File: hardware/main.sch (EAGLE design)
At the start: 37 parts, among them U1 TMS320F28069_PN_80, U10 TXB0101_DBV_6, U2 TXB0101_DBV_6, U3 TS3A5018_PW_16, U4 TS3A5018_PW_16, U5 SN74LVC4245A_DW_24, U7 Value, U8 Value, U9 SN74LVC4245A_DW_24

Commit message: Finished schematic, laid out board
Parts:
- removed EXTCON2: M10SILK_FEMALE_PTH, SparkFun-Connectors:M10SILK_FEMALE_PTH
- added JP3: M10SILK_FEMALE_PTH, SparkFun-Connectors:M10SILK_FEMALE_PTH
- added U$4, U$8: 8PIN_SOCKET, ControllerCard:8PIN_SOCKET
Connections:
- removed net IBUFIN1: U7.1A1
- removed net IBUFIN2: U7.1A2
- removed net IBUFIN3: U7.1A3
- removed net IBUFIN4: U7.1A4
- removed net IBUFIN5: U7.2A1
- removed net IBUFIN6: U7.2A2
- removed net IBUFIN7: U7.2A3
- removed net IBUFIN8: U7.2A4
- removed net OBUFIN1: U8.1Y1
- removed net OBUFIN2: U8.1Y2
- removed net OBUFIN3: U8.1Y3
- removed net OBUFIN4: U8.1Y4
- removed net OBUFIN5: U8.2Y1
- removed net OBUFIN6: U8.2Y2
- removed net OBUFIN7: U8.2Y3
- removed net OBUFIN8: U8.2Y4
- new net N$13: U$4.1, U8.1Y1
- new net N$14: U$4.2, U8.1Y2
- new net N$15: U$4.3, U8.1Y3
- new net N$16: U$4.4, U8.1Y4
- new net N$17: U$4.8, U8.2Y4
- new net N$18: U$4.7, U8.2Y3
- new net N$19: U$4.6, U8.2Y2
- new net N$20: U$4.5, U8.2Y1
- new net N$21: U$8.1, U7.1A1
- new net N$22: U$8.2, U7.1A2
- new net N$23: U$8.3, U7.1A3
- new net N$24: U$8.4, U7.1A4
- new net N$25: U$8.8, U7.2A4
- new net N$26: U$8.7, U7.2A3
- new net N$27: U$8.6, U7.2A2
- new net N$28: U$8.5, U7.2A1
- net !FLASHEN!: now also U1.GPIO22/EQEP1S/MCLKXA/SCITXDB; no longer U1.GPIO7/EPWM4B/SCIRXDA/ECAP2
- net !FLASHHOLD!: now also U1.GPIO33/SCLA/EPWMSYNCO/*ADCSOCBO; no longer U1.GPIO6/EPWM4A/EPWMSYNCI/EPWMSYNCO
- net !FLASHWP!: now also U1.GPIO32/SDAA/EPWMSYNCI/*ADCSOCAO; no longer U1.GPIO8/EPWM5A/*ADCSOCAO
- net 3.3V: no longer EXTCON2.1
- net 5V: now also JP3.10
- net BIN1: no longer EXTCON1.4
- net BIN2: no longer EXTCON1.6
- net BIN3: no longer EXTCON1.8
- net BIN4: no longer EXTCON1.10
- net BIN5: no longer EXTCON1.14
- net BIN6: no longer EXTCON1.16
- net BIN7: no longer EXTCON1.18
- net BIN8: no longer EXTCON1.20
- net GND: now also JP3.1; no longer EXTCON2.10
- net IBUFOUT1: now also EXTCON1.4
- net IBUFOUT2: now also EXTCON1.6
- net IBUFOUT3: now also EXTCON1.8
- net IBUFOUT4: now also EXTCON1.10
- net IBUFOUT5: now also EXTCON1.14
- net IBUFOUT6: now also EXTCON1.16
- net IBUFOUT7: now also EXTCON1.18
- net IBUFOUT8: now also EXTCON1.20
- net N$10: now also JP3.8
- net N$11: now also JP3.7
- net N$12: now also JP3.6
- net N$5: now also JP3.2
- net N$6: now also JP3.3
- net N$7: now also JP3.4
- net N$8: now also JP3.5
- net N$9: now also JP3.9
- net SPICLK: now also U1.GPIO14/*TZ3/SCITXDB/SPICLKB; no longer U1.GPIO18/SPICLKA/SCITXDB/XCLKOUT
- net SPISIMO: now also U1.GPIO24/ECAP1/SPISIMOB; no longer U1.GPIO16/SPISIMOA/*TZ2
- net SPISOMI: now also U1.GPIO13/*TZ2/SPISOMIB; no longer U1.GPIO17/SPISOMIA/*TZ3
- net UCIN1: now also U1.GPIO25/ECAP2/SPISOMIB; no longer U1.GPIO5/EPWM3B/SPISIMOA/ECAP1
- net UCIN2: now also U1.GPIO31/CANTXA/EPWM8A; no longer U1.GPIO25/ECAP2/SPISOMIB
- net UCIN3: now also U1.GPIO30/CANRXA/EPWM7A; no longer U1.GPIO31/CANTXA/EPWM8A
- net UCIN4: now also U1.GPIO29/SCITXDA/SCLA/*TZ3; no longer U1.GPIO30/CANRXA/EPWM7A
- net UCIN5: now also U1.GPIO12/*TZ1/SCITXDA/SPISIMOB; no longer U1.GPIO29/SCITXDA/SCLA/*TZ3
- net UCIN6: now also U1.GPIO9/EPWM5B/SCITXDB/ECAP3; no longer U1.GPIO12/*TZ1/SCITXDA/SPISIMOB
- net UCIN7: now also U1.GPIO28/SCIRXDA/SDAA/*TZ2; no longer U1.GPIO9/EPWM5B/SCITXDB/ECAP3
- net UCIN8: now also U1.GPIO18/SPICLKA/SCITXDB/XCLKOUT; no longer U1.GPIO28/SCIRXDA/SDAA/*TZ2
- net UCOUT1: now also U1.GPIO17/SPISOMIA/*TZ3; no longer EXTCON2.2, U1.GPIO3/EPWM2B/SPISOMIA/COMP2OUT
- net UCOUT2: now also U1.GPIO8/EPWM5A/*ADCSOCAO; no longer EXTCON2.3, U1.GPIO2/EPWM2A
- net UCOUT3: now also U1.GPIO16/SPISIMOA/*TZ2; no longer EXTCON2.4, U1.GPIO1/EPWM1B/COMP1OUT
- net UCOUT4: now also U1.GPIO7/EPWM4B/SCIRXDA/ECAP2; no longer EXTCON2.5, U1.GPIO0/EPWM1A
- net UCOUT5: now also U1.GPIO6/EPWM4A/EPWMSYNCI/EPWMSYNCO; no longer EXTCON2.6, U1.GPIO15/ECAP2/SCIRXDB/*SPISTEB
- net UCOUT6: now also U1.GPIO19/XCLKIN/*SPISTEA/SCIRXDB/ECAP1; no longer EXTCON2.7, U1.GPIO13/*TZ2/SPISOMIB
- net UCOUT7: now also U1.GPIO39; no longer EXTCON2.8, U1.GPIO14/*TZ3/SCITXDB/SPICLKB
- net UCOUT8: now also U1.GPIO11/EPWM6B/SCIRXDB/ECAP1; no longer EXTCON2.9, U1.GPIO24/ECAP1/SPISIMOB
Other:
- moved on the sheet: EXTCON1, R7, U10, U3, U4, U5, U7, U8, U9

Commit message: Began routing
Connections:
- net !FLASHEN!: now also U1.GPIO15/ECAP2/SCIRXDB/*SPISTEB; no longer U1.GPIO22/EQEP1S/MCLKXA/SCITXDB
- net !FLASHHOLD!: now also U1.GPIO22/EQEP1S/MCLKXA/SCITXDB; no longer U1.GPIO33/SCLA/EPWMSYNCO/*ADCSOCBO
- net !FLASHWP!: now also U1.GPIO0/EPWM1A; no longer U1.GPIO32/SDAA/EPWMSYNCI/*ADCSOCAO
- net ENEXT: now also U1.GPIO4/EPWM3A; no longer U1.GPIO20/EQEP1A/MDXA/COMP1OUT
- net RUNSEL: now also U1.GPIO20/EQEP1A/MDXA/COMP1OUT; no longer U1.GPIO23/EQEP1I/MFSXA/SCIRXDB
- net USBMON: now also U1.GPIO23/EQEP1I/MFSXA/SCIRXDB; no longer U1.GPIO10/EPWM6A/*ADCSOCBO
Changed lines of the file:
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@@
 <net name="USBMON" class="0">
-<segment>
-<pinref part="U1" gate="A" pin="GPIO10/EPWM6A/*ADCSOCBO"/>
-<wire x1="228.6" y1="144.78" x2="233.68" y2="144.78" width="0.1524" layer="91"/>
-<label x="233.68" y="144.78" size="1.016" layer="95" xref="yes"/>
-</segment>
 <segment>
 <pinref part="U2" gate="A" pin="A"/>
@@
 <wire x1="375.92" y1="68.58" x2="373.38" y2="68.58" width="0.1524" layer="91"/>
 <label x="373.38" y="68.58" size="1.016" layer="95" rot="R180" xref="yes"/>
+</segment>
+<segment>
+<pinref part="U1" gate="A" pin="GPIO23/EQEP1I/MFSXA/SCIRXDB"/>
+<wire x1="228.6" y1="109.22" x2="233.68" y2="109.22" width="0.1524" layer="91"/>
+<label x="233.68" y="109.22" size="1.016" layer="95" xref="yes"/>
 </segment>
 </net>
@@
 </segment>
 <segment>
-<pinref part="U1" gate="A" pin="GPIO20/EQEP1A/MDXA/COMP1OUT"/>
-<wire x1="45.72" y1="22.86" x2="40.64" y2="22.86" width="0.1524" layer="91"/>
-<label x="40.64" y="22.86" size="1.016" layer="95" rot="R180" xref="yes"/>
-</segment>
-<segment>
 <pinref part="U10" gate="A" pin="OE"/>
 <pinref part="R7" gate="G$1" pin="2"/>
@@
 <label x="254" y="271.78" size="1.016" layer="95" xref="yes"/>
 </segment>
+<segment>
+<pinref part="U1" gate="A" pin="GPIO4/EPWM3A"/>
+<wire x1="228.6" y1="35.56" x2="233.68" y2="35.56" width="0.1524" layer="91"/>
+<label x="233.68" y="35.56" size="1.016" layer="95" xref="yes"/>
+</segment>
 </net>
 <net name="SPICLK" class="0">
@@
 </segment>
 <segment>
+<pinref part="U1" gate="A" pin="GPIO15/ECAP2/SCIRXDB/*SPISTEB"/>
+<wire x1="228.6" y1="83.82" x2="233.68" y2="83.82" width="0.1524" layer="91"/>
+<label x="233.68" y="83.82" size="1.016" layer="95" xref="yes"/>
+</segment>
+</net>
+<net name="!FLASHWP!" class="0">
+<segment>
+<pinref part="U$6" gate="G$1" pin="!WP!"/>
+<wire x1="424.18" y1="152.4" x2="429.26" y2="152.4" width="0.1524" layer="91"/>
+<label x="429.26" y="152.4" size="1.016" layer="95" xref="yes"/>
+</segment>
+<segment>
+<pinref part="U1" gate="A" pin="GPIO0/EPWM1A"/>
+<wire x1="228.6" y1="40.64" x2="233.68" y2="40.64" width="0.1524" layer="91"/>
+<label x="233.68" y="40.64" size="1.016" layer="95" xref="yes"/>
+</segment>
+</net>
+<net name="!FLASHHOLD!" class="0">
+<segment>
+<pinref part="U$6" gate="G$1" pin="!HOLD!"/>
+<wire x1="424.18" y1="149.86" x2="429.26" y2="149.86" width="0.1524" layer="91"/>
+<label x="429.26" y="149.86" size="1.016" layer="95" xref="yes"/>
+</segment>
+<segment>
 <pinref part="U1" gate="A" pin="GPIO22/EQEP1S/MCLKXA/SCITXDB"/>
 <wire x1="228.6" y1="114.3" x2="233.68" y2="114.3" width="0.1524" layer="91"/>
 <label x="233.68" y="114.3" size="1.016" layer="95" xref="yes"/>
-</segment>
-</net>
-<net name="!FLASHWP!" class="0">
-<segment>
-<pinref part="U$6" gate="G$1" pin="!WP!"/>
-<wire x1="424.18" y1="152.4" x2="429.26" y2="152.4" width="0.1524" layer="91"/>
-<label x="429.26" y="152.4" size="1.016" layer="95" xref="yes"/>
-</segment>
-<segment>
-<pinref part="U1" gate="A" pin="GPIO32/SDAA/EPWMSYNCI/*ADCSOCAO"/>
-<wire x1="228.6" y1="139.7" x2="233.68" y2="139.7" width="0.1524" layer="91"/>
-<label x="233.68" y="139.7" size="1.016" layer="95" xref="yes"/>
-</segment>
-</net>
-<net name="!FLASHHOLD!" class="0">
-<segment>
-<pinref part="U$6" gate="G$1" pin="!HOLD!"/>
-<wire x1="424.18" y1="149.86" x2="429.26" y2="149.86" width="0.1524" layer="91"/>
-<label x="429.26" y="149.86" size="1.016" layer="95" xref="yes"/>
-</segment>
-<segment>
-<pinref part="U1" gate="A" pin="GPIO33/SCLA/EPWMSYNCO/*ADCSOCBO"/>
-<wire x1="228.6" y1="147.32" x2="233.68" y2="147.32" width="0.1524" layer="91"/>
-<label x="233.68" y="147.32" size="1.016" layer="95" xref="yes"/>
 </segment>
 </net>
@@
 </segment>
 <segment>
-<pinref part="U1" gate="A" pin="GPIO23/EQEP1I/MFSXA/SCIRXDB"/>
-<wire x1="228.6" y1="109.22" x2="233.68" y2="109.22" width="0.1524" layer="91"/>
-<label x="233.68" y="109.22" size="1.016" layer="95" xref="yes"/>
-</segment>
-</net>
+<pinref part="U1" gate="A" pin="GPIO20/EQEP1A/MDXA/COMP1OUT"/>
+<wire x1="45.72" y1="22.86" x2="40.64" y2="22.86" width="0.1524" layer="91"/>
+<label x="40.64" y="22.86" size="1.016" layer="95" rot="R180" xref="yes"/>
+</segment>
+</net>

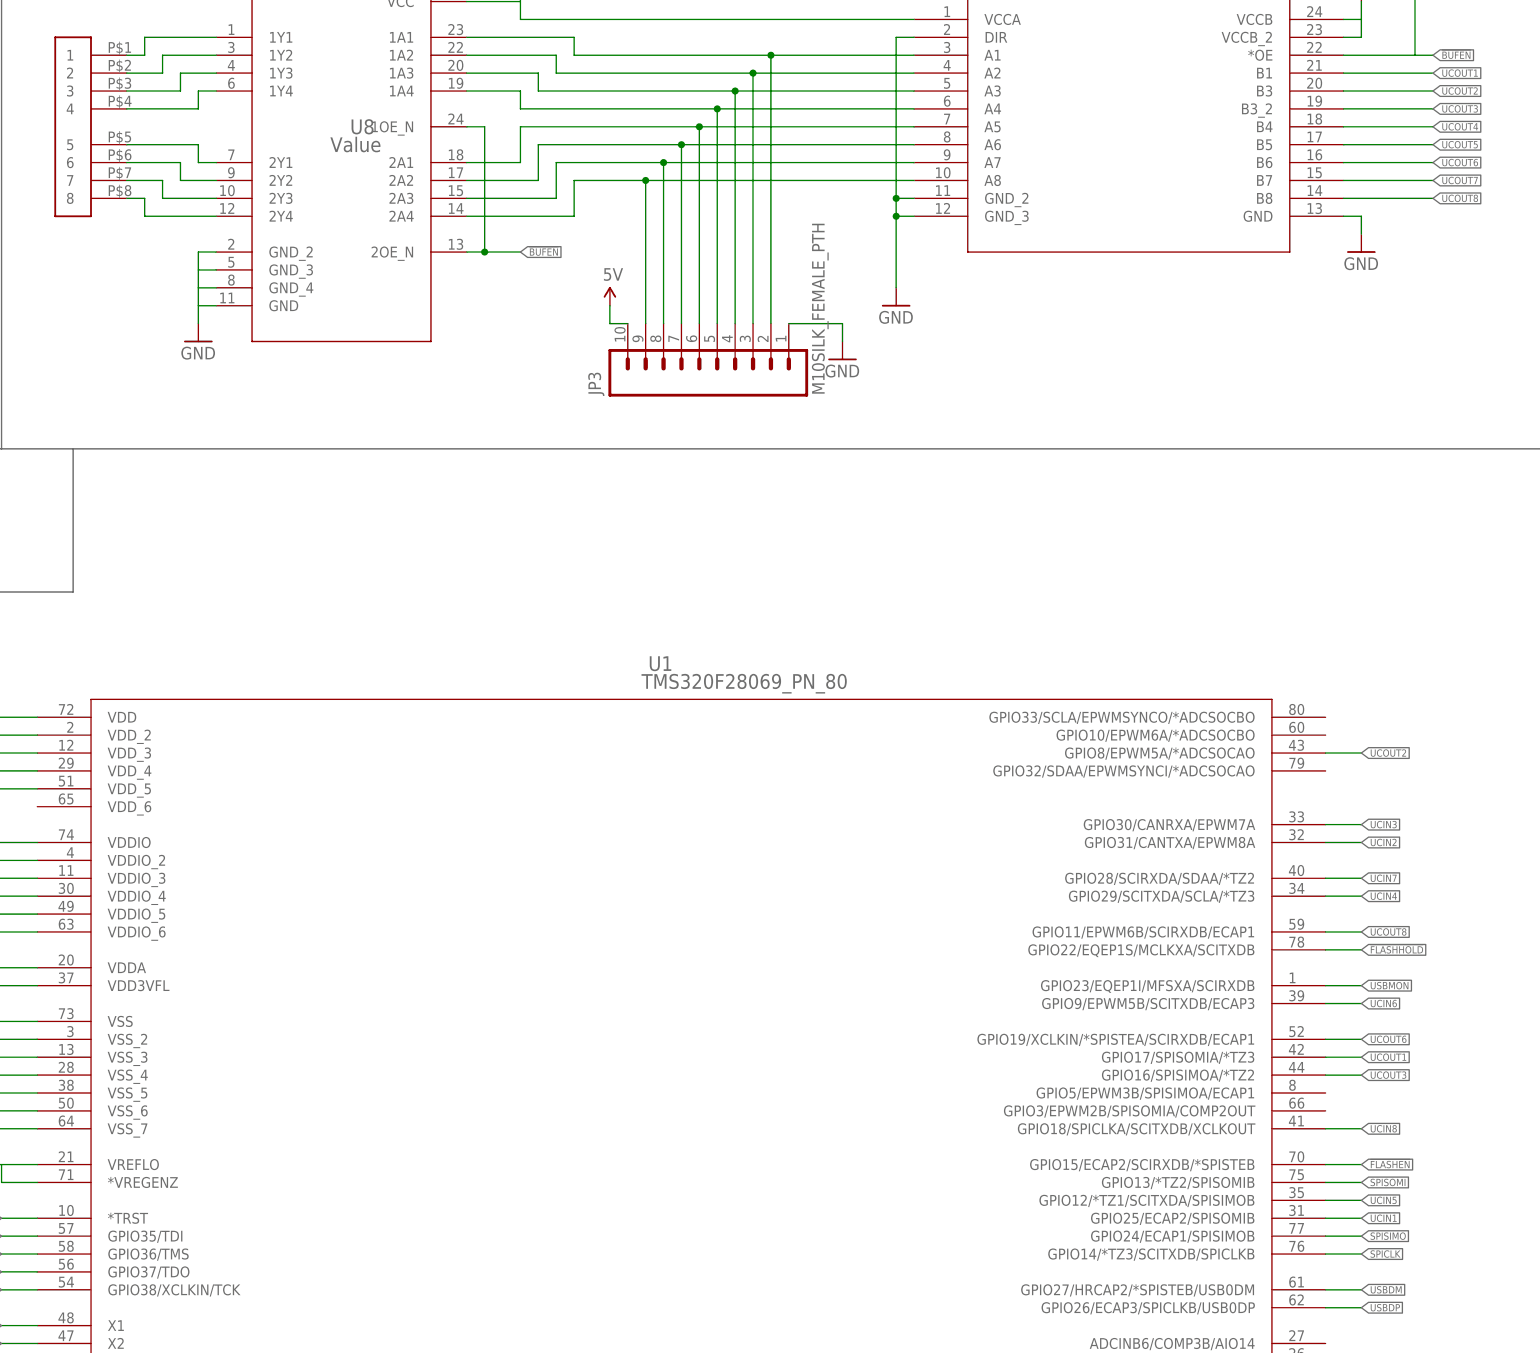
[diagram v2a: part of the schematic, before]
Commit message: Finished routing SPI Flash and Output section. Re-wired parts of the input section.
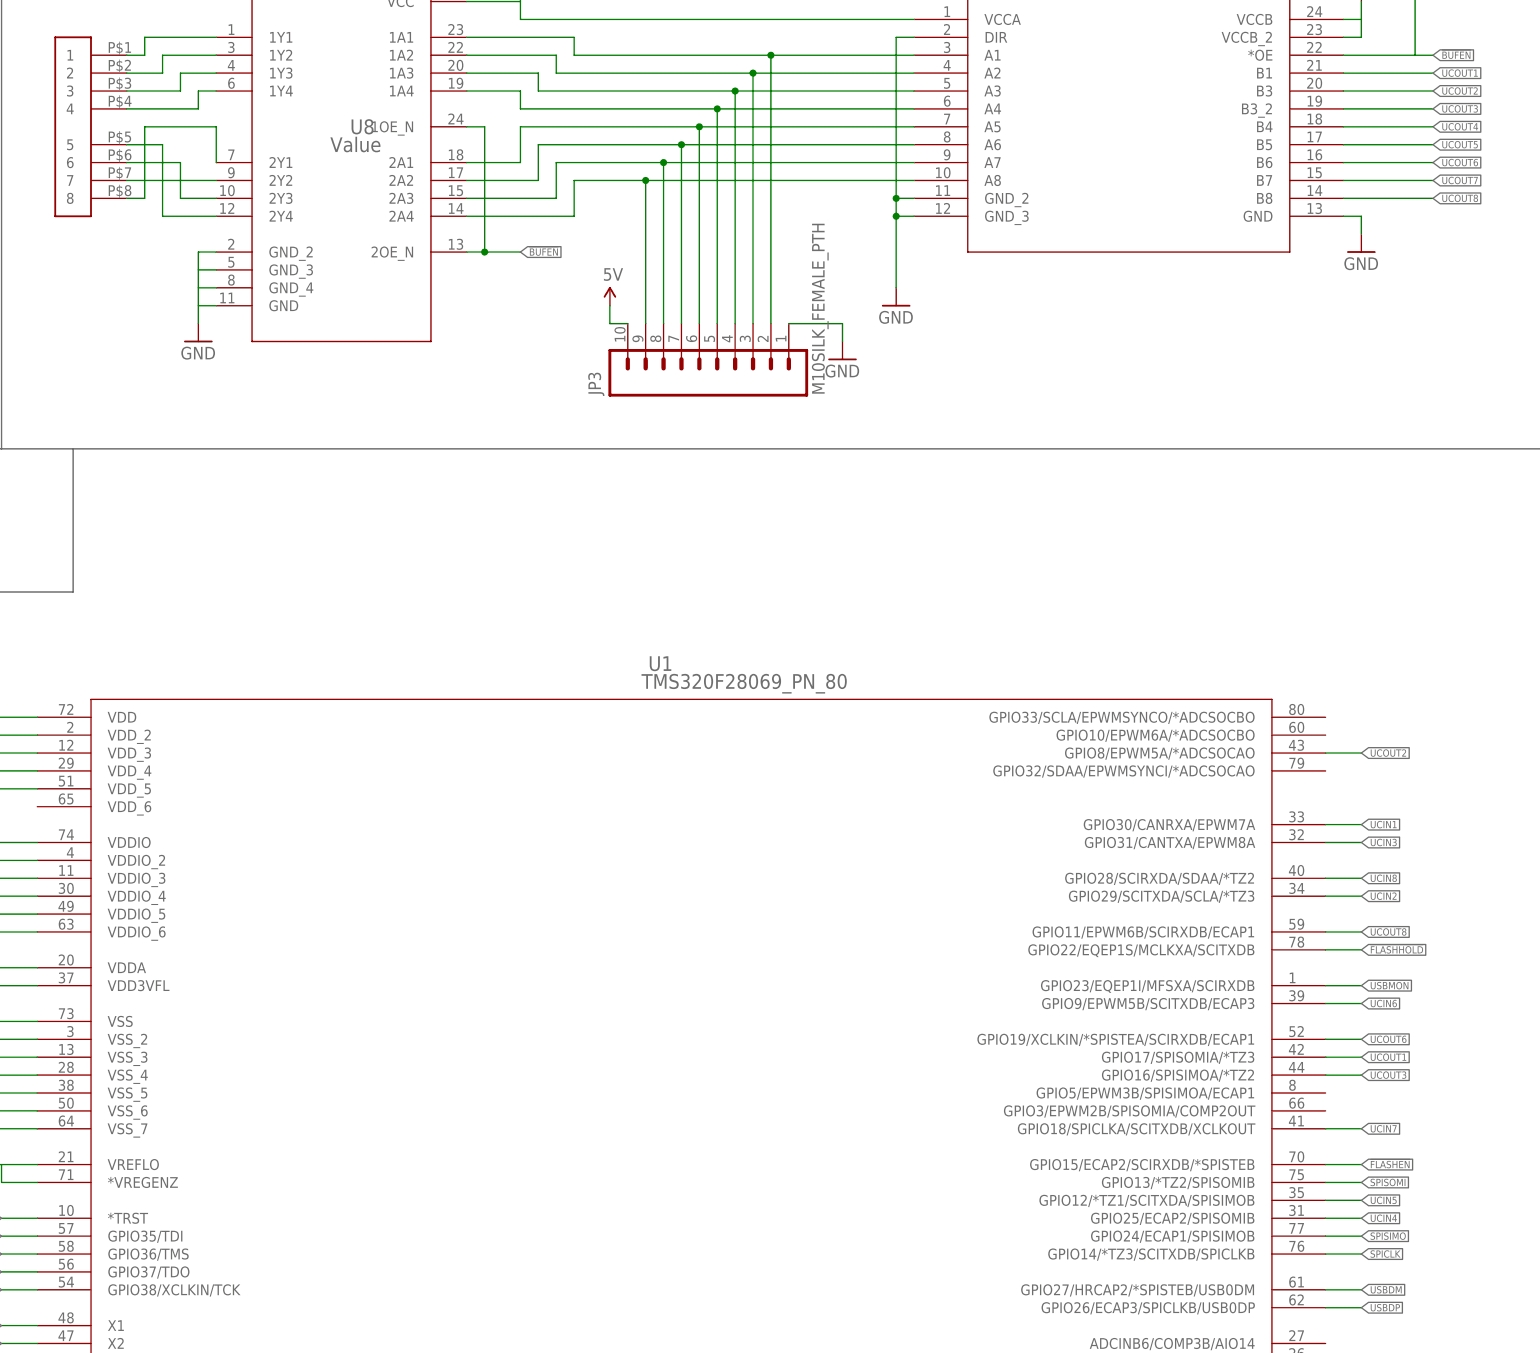
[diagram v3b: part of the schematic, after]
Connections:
- net N$17: now also U$4.5; no longer U$4.8
- net N$18: now also U$4.6; no longer U$4.7
- net N$19: now also U$4.7; no longer U$4.6
- net N$20: now also U$4.8; no longer U$4.5
- net UCIN1: now also U1.GPIO30/CANRXA/EPWM7A; no longer U1.GPIO25/ECAP2/SPISOMIB
- net UCIN2: now also U1.GPIO29/SCITXDA/SCLA/*TZ3; no longer U1.GPIO31/CANTXA/EPWM8A
- net UCIN3: now also U1.GPIO31/CANTXA/EPWM8A; no longer U1.GPIO30/CANRXA/EPWM7A
- net UCIN4: now also U1.GPIO25/ECAP2/SPISOMIB; no longer U1.GPIO29/SCITXDA/SCLA/*TZ3
- net UCIN7: now also U1.GPIO18/SPICLKA/SCITXDB/XCLKOUT; no longer U1.GPIO28/SCIRXDA/SDAA/*TZ2
- net UCIN8: now also U1.GPIO28/SCIRXDA/SDAA/*TZ2; no longer U1.GPIO18/SPICLKA/SCITXDB/XCLKOUT
